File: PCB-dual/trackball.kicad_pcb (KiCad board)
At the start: 2 copper layers, 48.8 x 42.5 mm, 8 parts, among them J3 Conn_01x01_Male, Q1 MMBT2222A-7-F, U1 Adafruit_QT_Py_M0, U2 MrJohnK_PMW3360DM-T2QU, U3 MrJohnK_PMW3360DM-T2QU

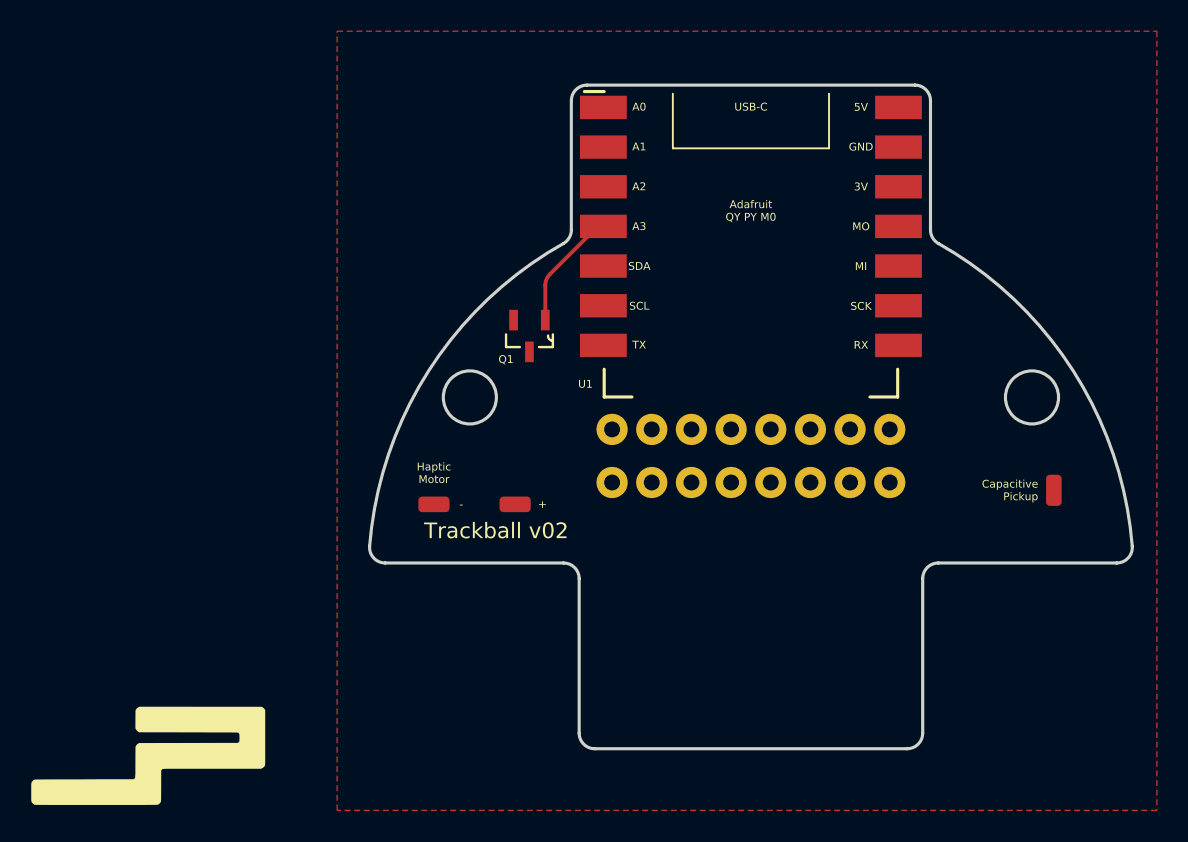
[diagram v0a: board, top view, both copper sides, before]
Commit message: feat: first draft of v02 trackball with dual sensor support, fixes to footprints and OSHPark gerber .zip not yet tested
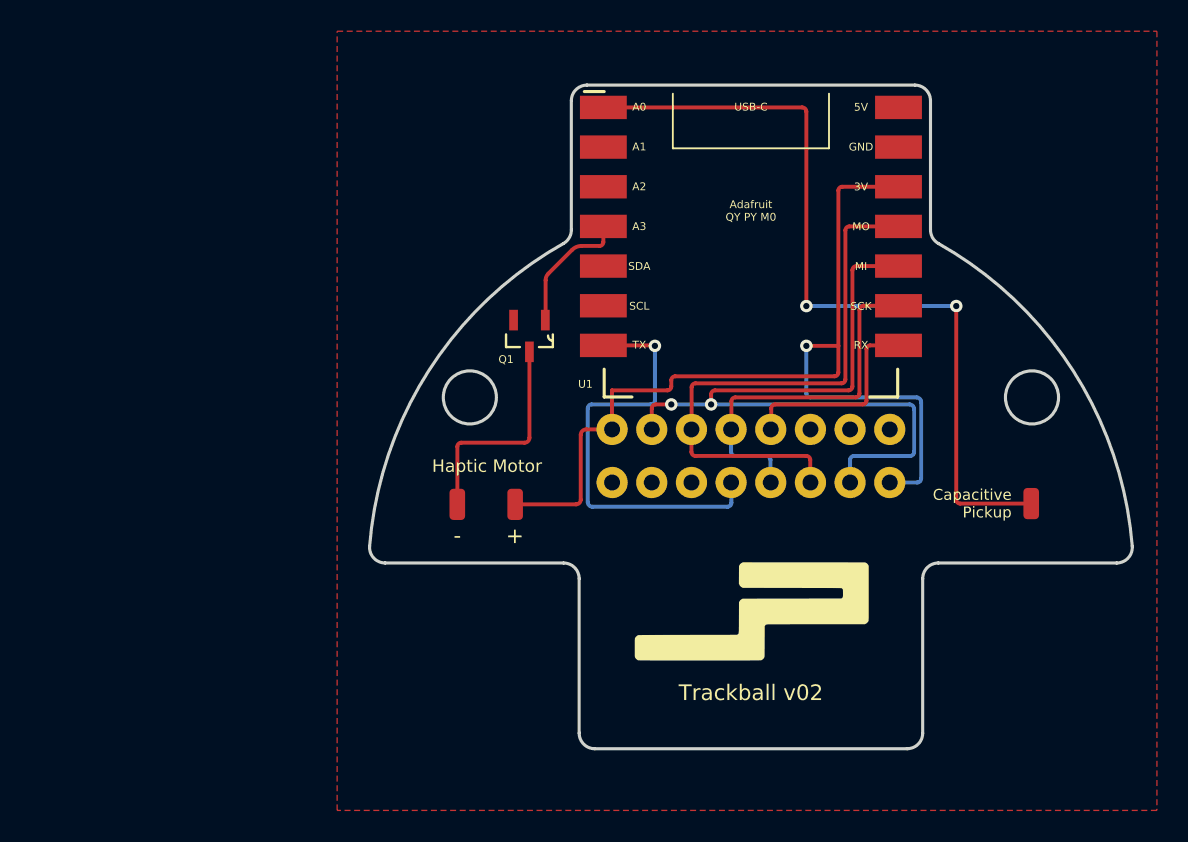
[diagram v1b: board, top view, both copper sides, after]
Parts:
- moved G*** 39.7 mm to (144.6, 155.7)
- moved J3 1.68 mm to (162.4, 148.8)
- moved - 1.50 mm to (125.7, 148.8), turned to 0 degrees
- turned + to 0 degrees
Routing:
- net Net-(J1-Pad1): track 0.00 -> 63.9 mm, vias 0 -> 1
- net Net-(J3-Pad1): track 0.00 -> 52.5 mm, vias 0 -> 2
- net Net-(U1-Pad12): track 0.00 -> 47.5 mm, vias 0 -> 2
- net Net-(U1-Pad11): track 0.00 -> 36.7 mm
- net Net-(U1-Pad7): track 0.00 -> 28.2 mm, vias 0 -> 1
- net Net-(U1-Pad13): track 0.00 -> 24.0 mm
- net Net-(J2-Pad1): track 0.00 -> 14.1 mm
- net Net-(U1-Pad14): track 0.00 -> 13.2 mm
- net Net-(Q1-Pad1): track 7.70 -> 8.40 mm

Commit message: feat: cleaned up tracks minimizing crossover on F/B layers, simplified some tracks, ground plane now on both sides
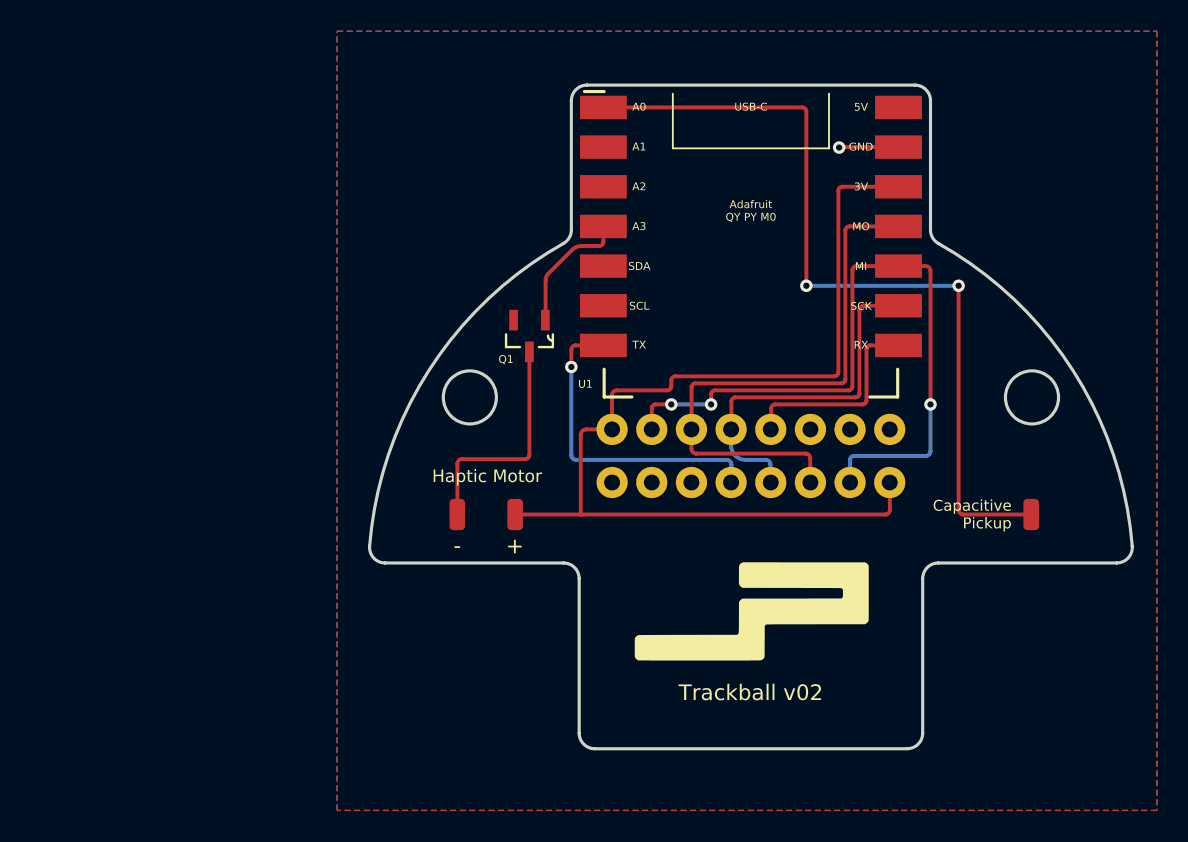
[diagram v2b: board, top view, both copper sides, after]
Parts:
- moved J3 0.70 mm to (162.4, 149.4)
- moved + 0.65 mm to (129.4, 149.4)
- moved - 0.65 mm to (125.7, 149.4)
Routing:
- net Net-(U1-Pad7): track 28.2 -> 20.7 mm
- net GND: track 0.00 -> 3.82 mm, vias 0 -> 1
- net Net-(J1-Pad1): track 63.9 -> 66.5 mm, vias 1 -> 0
- net Net-(U1-Pad12): track 47.5 -> 46.4 mm, vias 2 -> 3
- net Net-(J3-Pad1): track 52.5 -> 53.2 mm
- net Net-(J2-Pad1): track 14.1 -> 14.8 mm
- added copper zone on B.Cu, net GND
